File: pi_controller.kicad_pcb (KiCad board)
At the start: 4 copper layers, 99.7 x 91.3 mm, 153 parts, among them J1 PWM, J10 AN4, J11 AN6, J12 AN8, J13 AN10, J14 AN14, J15 AN15, J16 AN2, J17 CS2, J18 CS4, J19 CS6, J2 DC Supply, J20 CS8, J21 CS3, J22 CS5, J23 CS7, J24 AN1, J25 AN16, J26 LED6, J27 LED5, J28 LED7, J29 LED8, J3 AN12, J30 I2C, J31 UART, J32 LED3, J33 LED1, J34 LED2, J35 LED4, J36 ROW1, J37 ROW2, J38 ROW3, J39 ROW5, J4 AN7, J40 ROW4, J41 ROW6, J42 ROW7, J43 ROW8, J5 AN9, J6 AN11, J7 AN5, J8 AN3, J9 AN13, Q1 AOD4184A, U1 AP62300TWU, U2 CD74HC4067SM96, U3 LM4040DBZ-3, U4 RaspberryPi_Pico, U5 74HC138, U6 TM1639 (TA2009B), U7 74HC138

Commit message: Layout ground pour and other adjustments
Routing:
- net /COL_MUX_C: track 126.8 -> 125.2 mm
- net /COL_MUX_B: track 133.2 -> 134.6 mm
- net /MISO: track 74.9 -> 73.8 mm
- net /COL1: track 85.5 -> 86.4 mm
- net /COL3: track 82.2 -> 82.9 mm
- net /UART0_TX: track 21.5 -> 22.2 mm
- net /MOSI: track 122.1 -> 122.6 mm
- net GND: track 36.4 -> 36.6 mm, vias 49 -> 74
- added copper zone on B.Cu, net GND

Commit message: Refining layout
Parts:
- added G***: LOGO, pi_controller:logo-pimatrix, B.Cu at (105.5, 84.5)
- renumbered J24 to AN1, J13 to AN10, J6 to AN11, J3 to AN12, J9 to AN13, J14 to AN14, J15 to AN15, J25 to AN16, J16 to AN2, J8 to AN3, J10 to AN4, J7 to AN5, J11 to AN6, J4 to AN7, J12 to AN8, J5 to AN9
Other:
- board text added: "9V / 2A"

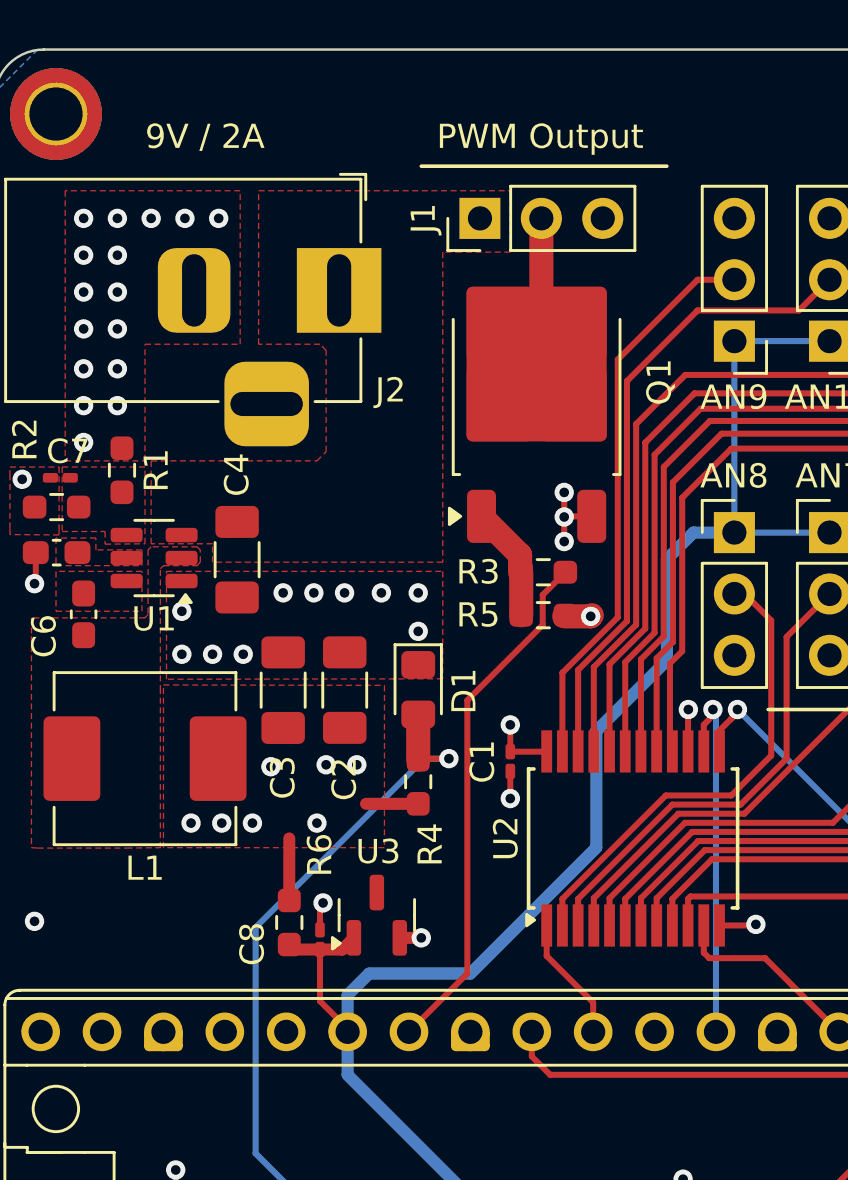
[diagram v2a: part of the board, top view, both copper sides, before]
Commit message: Improving PWM circuit
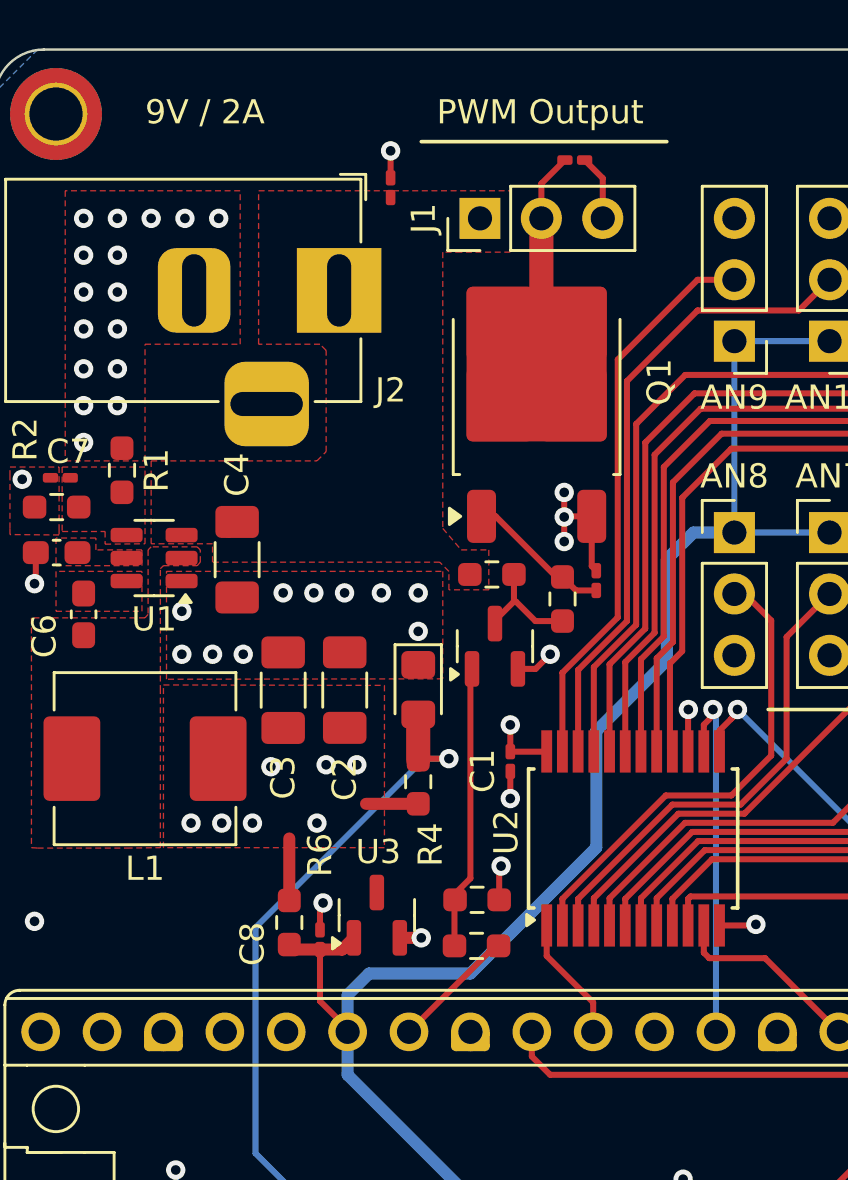
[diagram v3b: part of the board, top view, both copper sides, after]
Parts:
- added C13: 0.1uF, Capacitor_SMD:C_0201_0603Metric_Pad0.64x0.40mm_HandSolder, F.Cu at (113.2, 60.7)
- added C14: 1nF, Capacitor_SMD:C_0201_0603Metric_Pad0.64x0.40mm_HandSolder, F.Cu at (114.0, 78.1)
- added C15: 100uF, Capacitor_SMD:C_0201_0603Metric_Pad0.64x0.40mm_HandSolder, F.Cu at (105.5, 61.8)
- added Q2: MMBT3904, Package_TO_SOT_SMD:SOT-23, F.Cu at (109.9, 80.8)
- added R17: 2.2k, Resistor_SMD:R_0603_1608Metric_Pad0.98x0.95mm_HandSolder, F.Cu at (109.1, 93.2)
- added R18: 10R, Resistor_SMD:R_0603_1608Metric_Pad0.98x0.95mm_HandSolder, F.Cu at (112.6, 78.9)
- R3: value 100 -> 1.5k
- moved R5 12.1 mm to (109.1, 91.3)
- moved R3 2.13 mm to (109.7, 77.9), turned to 180 degrees
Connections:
- Q1 pad 1: Net-(Q1-Pad1) -> Net-(C14-Pad1)
- R3 pad 1: Net-(Q1-Pad1) -> Net-(Q2-C)
- R3 pad 2: /PWM_OUT -> +9V
- R5 pad 2: Net-(Q1-Pad1) -> Net-(Q2-B)
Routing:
- net /PWM_OUT: track 21.7 -> 5.18 mm
- net Net-(Q2-B): track 0.00 -> 11.8 mm
- net GND: track 36.6 -> 44.6 mm, vias 74 -> 76
- net Net-(C14-Pad1): track 0.00 -> 6.02 mm
- net Net-(Q1-Pad1): track 4.77 -> 0.00 mm
- net Net-(Q2-C): track 0.00 -> 4.77 mm
- net Net-(J1-Pin_2): track 6.11 -> 8.93 mm

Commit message: Adjusting components
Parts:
- renumbered J36 to JR1, J37 to JR2, J38 to JR3, J40 to JR4, J39 to JR5, J41 to JR6, J42 to JR7, J43 to JR8
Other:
- board text added: "(4.2V to 18V)"
- board text added: "0.1500 mm / 0.1500 mm"
- board text added: "0.2500 mm"
- board text added: "1.6000 mm"
- board text added: "4"
- board text added: "99.6950 mm x 91.3130 mm"
- board text added: "BOARD CHARACTERISTICS"
- board text added: "Board Thickness:"
- board text added: "Board overall dimensions:"
- board text added: "Castellated pads:"
- board text added: "Copper Finish:"
- board text added: "Copper Layer Count:"
- board text added: "Edge card connectors:"
- board text added: "GND"
- board text added: "HAL lead-free"
- board text added: "Impedance Control:"
- board text added: "LED"
- board text added: "Min hole diameter:"
- board text added: "Min track/spacing:"
- board text added: "No"
- board text added: "Plated Board Edge:"
- board text added: "REV 1"
- board text added: "VDD"
- board text added: "VDDA"
- board text added: "Vin 9V"
- board text added: "Yes"
- board text removed: "9V / 2A"
